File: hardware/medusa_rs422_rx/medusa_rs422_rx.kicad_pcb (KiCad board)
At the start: 2 copper layers, 42 x 50 mm, 16 parts, among them J1 HEADER_2X3, P1 RJ45X1, P2 RJ45X1, P3 BARRIER2, U1 UA9637A

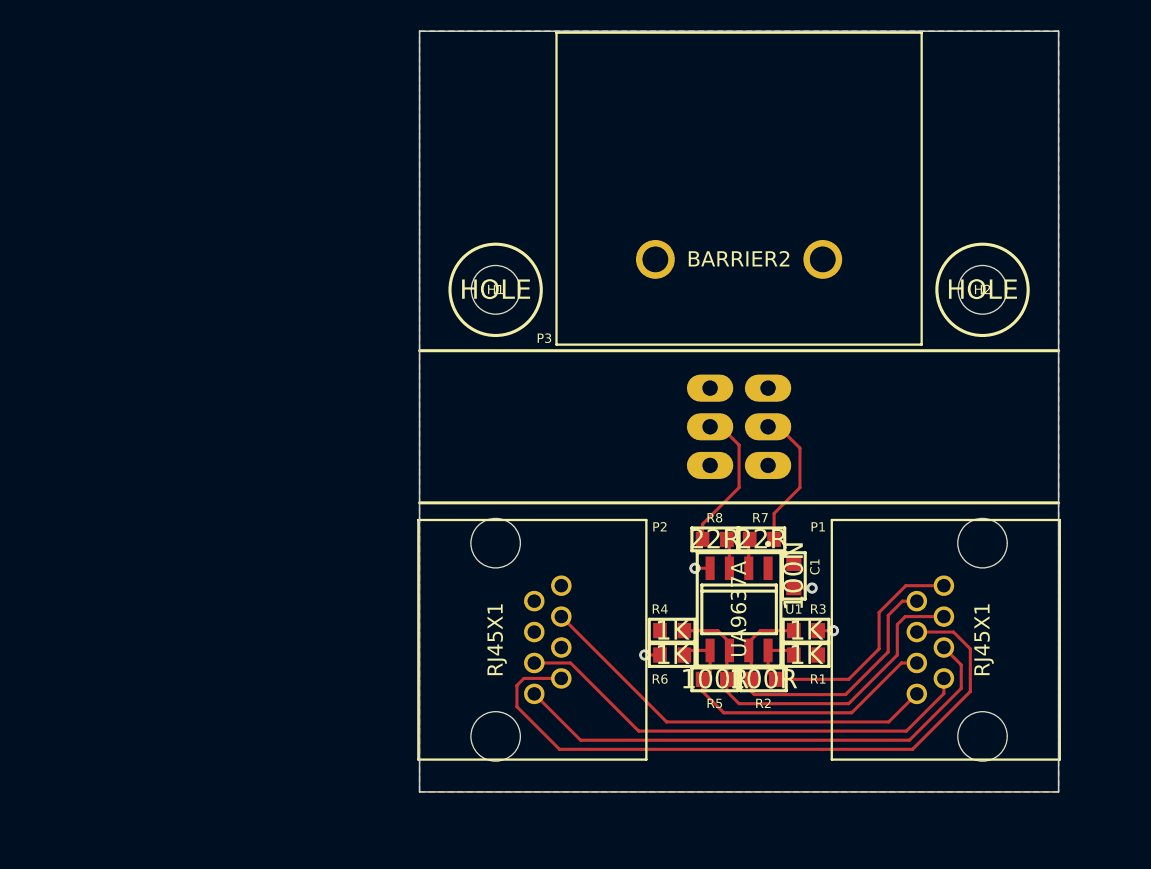
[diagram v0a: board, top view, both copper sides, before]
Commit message: Complete rebake of RX board.
Added ground isolation.
Changed receiver IC to better match transmitter specs.
Added somewhat sketchy termination + ground reference mechanism.
Removed RJ45 connectors and passthrough in favor of a single board with four channels and terminal blocks.
Added separate terminal blocks for power supply (+5V) and isolated power connections. If we run dedicated ground reference wires from the transmitters, this is where they'll connect.
Added optional power regulator for 3.3V operation, if we want to experiment with MCUs at the receivers.
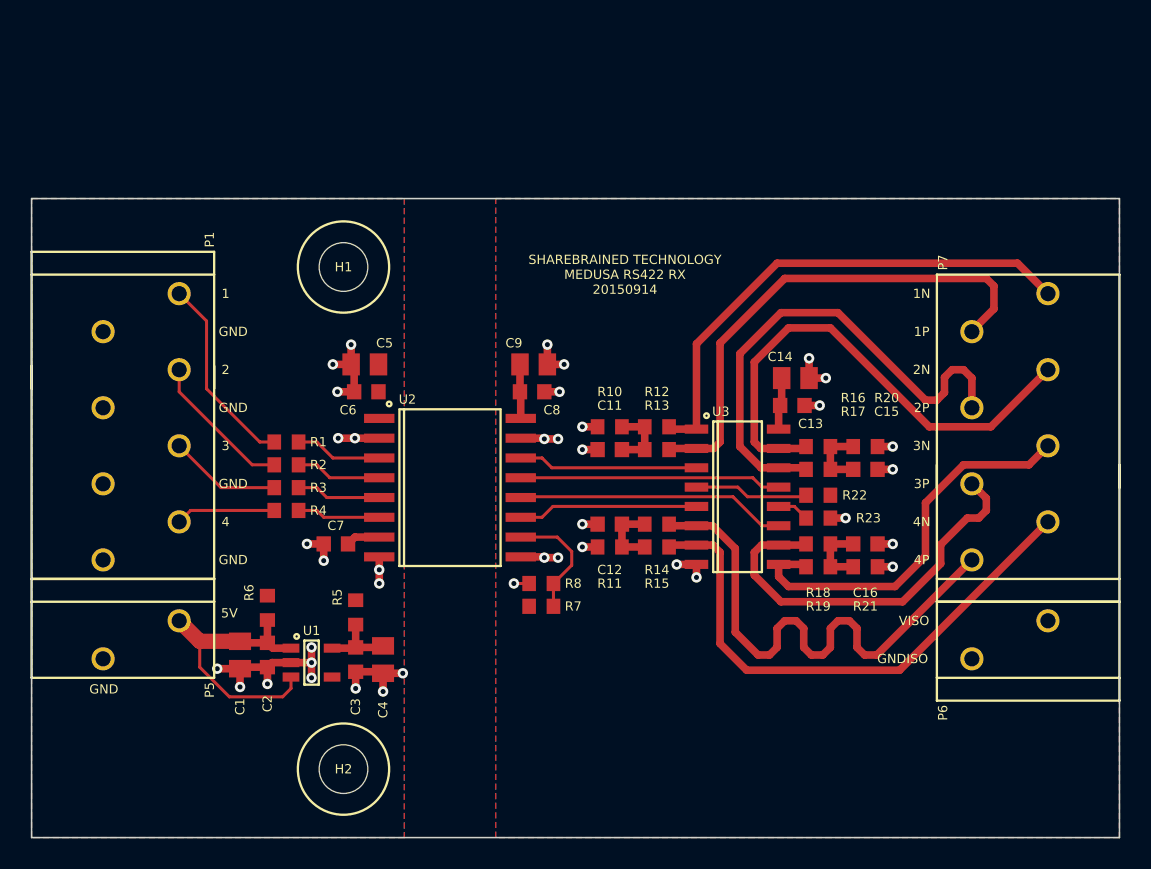
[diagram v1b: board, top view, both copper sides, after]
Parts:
- removed J1: HEADER_2X3, LED_STRIP_WS2812
- removed P2: RJ45X1, AMPHENOL_RJHSE5080
- removed P3: BARRIER2, ONSHORE_OSTYK55102030
- added C11: 10N, ipc_capc:IPC_CAPC1608X95N, F.Cu at (140.5, 101.5)
- added C12: 10N, ipc_capc:IPC_CAPC1608X95N, F.Cu at (140.5, 106.4)
- added C13: 100N, ipc_capc:IPC_CAPC1608X95N, F.Cu at (152.5, 98.6)
- added C14: 10U, ipc_capc:IPC_CAPC2012X140N, F.Cu at (152.7, 96.8)
- added C15: 10N, ipc_capc:IPC_CAPC1608X95N, F.Cu at (157.3, 102.8)
- added C16: 10N, ipc_capc:IPC_CAPC1608X95N, F.Cu at (157.3, 107.7)
- added C2: DNI, ipc_capc:IPC_CAPC1608X95N, F.Cu at (118.0, 115.0)
- added C3: DNI, ipc_capc:IPC_CAPC1608X95N, F.Cu at (123.8, 115.3)
- added C4: DNI, ipc_capc:IPC_CAPC2012X140N, F.Cu at (125.6, 115.3)
- added C5: 10U, ipc_capc:IPC_CAPC2012X140N, F.Cu at (124.4, 95.9)
- added C6: 100N, ipc_capc:IPC_CAPC1608X95N, F.Cu at (124.5, 97.7)
- added C7: 100N, ipc_capc:IPC_CAPC1608X95N, F.Cu at (122.5, 107.7)
- added C8: 100N, ipc_capc:IPC_CAPC1608X95N, F.Cu at (135.4, 97.7)
- added C9: 10U, ipc_capc:IPC_CAPC2012X140N, F.Cu at (135.5, 95.9)
- added P5: TERM2, phoenix:1990009, F.Cu at (108.5, 114.0)
- added P6: TERM2, phoenix:1990009, F.Cu at (168.0, 114.0)
- added P7: TERM8, phoenix:1990067, F.Cu at (168.0, 100.0)
- added R10: DNI, ipc_resc:IPC_RESC1608X55N, F.Cu at (140.5, 100.0)
- added R11: DNI, ipc_resc:IPC_RESC1608X55N, F.Cu at (140.5, 107.9)
- added R12: 50R, ipc_resc:IPC_RESC1608X55N, F.Cu at (143.6, 100.0)
- added R13: 50R, ipc_resc:IPC_RESC1608X55N, F.Cu at (143.6, 101.5)
- added R14: 50R, ipc_resc:IPC_RESC1608X55N, F.Cu at (143.6, 106.4)
- added R15: 50R, ipc_resc:IPC_RESC1608X55N, F.Cu at (143.6, 107.9)
- added R16: 50R, ipc_resc:IPC_RESC1608X55N, F.Cu at (154.2, 101.3)
- added R17: 50R, ipc_resc:IPC_RESC1608X55N, F.Cu at (154.2, 102.8)
- added R18: 50R, ipc_resc:IPC_RESC1608X55N, F.Cu at (154.2, 107.7)
- added R19: 50R, ipc_resc:IPC_RESC1608X55N, F.Cu at (154.2, 109.2)
- added R20: DNI, ipc_resc:IPC_RESC1608X55N, F.Cu at (157.3, 101.3)
- added R21: DNI, ipc_resc:IPC_RESC1608X55N, F.Cu at (157.3, 109.2)
- added R22: 0R, ipc_resc:IPC_RESC1608X55N, F.Cu at (154.2, 104.5)
- added R23: 0R, ipc_resc:IPC_RESC1608X55N, F.Cu at (154.2, 106.0)
- added U2: ADuM6404, ipc_soic:IPC_SOIC127P1030X265-16N, F.Cu at (130.0, 104.0)
- added U3: AM26LV32E, ipc_soic:IPC_SOIC127P600X175-16N, F.Cu at (148.9, 104.6)
- C1: value 100N -> DNI; footprint IPC_CAPC1608X95N -> ipc_capc:IPC_CAPC2012X140N
- H1, H2: footprint HOLE_3P2MM -> hole:HOLE_3P2MM
- P1: value RJ45X1 -> TERM8; footprint AMPHENOL_RJHSE5080 -> phoenix:1990067
- R1, R3, R4: value 1K -> 22R; footprint IPC_RESC1608X55N -> ipc_resc:IPC_RESC1608X55N
- R2: value 100R -> 22R; footprint IPC_RESC1608X55N -> ipc_resc:IPC_RESC1608X55N
- R5: value 100R -> DNI; footprint IPC_RESC1608X55N -> ipc_resc:IPC_RESC1608X55N
- R6: value 1K -> 0R; footprint IPC_RESC1608X55N -> ipc_resc:IPC_RESC1608X55N
- R7: value 22R -> DNI; footprint IPC_RESC1608X55N -> ipc_resc:IPC_RESC1608X55N
- R8: value 22R -> 0R; footprint IPC_RESC1608X55N -> ipc_resc:IPC_RESC1608X55N
- U1: value UA9637A -> DNI; footprint IPC_SOIC127P600X175-8N -> ipc_sot:IPC_SOT95P280X110-5N
- moved P1 58.2 mm to (108.5, 100.0), turned to 270 degrees
- moved H2 52.5 mm to (123.0, 122.5)
- moved R1 36.9 mm to (119.2, 101.0), turned to 180 degrees
- moved C1 36.8 mm to (116.2, 115.0)
- moved R3 35.4 mm to (119.2, 104.0)
- moved R2 34.4 mm to (119.2, 102.5), turned to 180 degrees
- moved U1 28.3 mm to (120.9, 115.5), turned to 0 degrees
- moved R6 26.8 mm to (118.0, 111.9), turned to 270 degrees
- moved R4 26.6 mm to (119.2, 105.5)
- moved R5 24.0 mm to (123.8, 112.2), turned to 270 degrees
- moved R7 15.2 mm to (136.0, 111.8), turned to 180 degrees
- moved R8 11.8 mm to (136.0, 110.3)
- moved H1 10.1 mm to (123.0, 89.5)
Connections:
- P1 pad 1: /RX1P -> GND
- P1 pad 2: /RX1N -> /RX4R
- P1 pad 3: /RX2P -> GND
- P1 pad 4: /PT1N -> /RX3R
- P1 pad 5: /PT1P -> GND
- P1 pad 6: /RX2N -> /RX2R
- P1 pad 7: /PT2P -> GND
- P1 pad 8: /PT2N -> /RX1R
- R1 pad 1: /RX1P -> /RX1
- R1 pad 2: +5V -> /RX1R
- R2 pad 1: /RX1N -> /RX2
- R2 pad 2: /RX1P -> /RX2R
- R3 pad 1: GND -> /RX3
- R3 pad 2: /RX1N -> /RX3R
- R4 pad 1: /RX2P -> /RX4
- R4 pad 2: +5V -> /RX4R
- R5 pad 1: /RX2N -> /VDD1
- R5 pad 2: /RX2P -> +3.3V
- R6 pad 1: GND -> /VDD1
- R6 pad 2: /RX2N -> +5V
- R7 pad 1: Net-<R7-Pad1> -> /VSEL
- R7 pad 2: /DI_B -> /VISO
- R8 pad 1: Net-<R8-Pad1> -> /VSEL
- R8 pad 2: /DI_A -> /GNDISO
- U1 pad 2: Net-<R7-Pad1> -> GND
- U1 pad 3: Net-<R8-Pad1> -> +5V
- U1 pad 4: GND -> (no net)
- U1 pad 5: /RX2N -> +3.3V
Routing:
- net /PT1N: track 43.8 -> 0.00 mm
- net /RX4P: track 0.00 -> 35.9 mm
- net /RX4N: track 0.00 -> 35.9 mm
- net /PT1P: track 33.9 -> 0.00 mm
- net /PT2P: track 30.8 -> 0.00 mm
- net /PT2N: track 27.0 -> 0.00 mm
- net /RX3N: track 0.00 -> 26.5 mm
- net /RX3P: track 0.00 -> 26.5 mm
- net GND: track 4.19 -> 28.2 mm, vias 4 -> 18
- net /GNDISO: track 0.00 -> 23.9 mm, vias 0 -> 22
- net +5V: track 0.00 -> 19.1 mm
- net /RX3ISO: track 0.00 -> 17.8 mm
- net /RX2ISO: track 0.00 -> 17.2 mm
- net /RX1P: track 18.9 -> 33.6 mm
- net /RX1R: track 0.00 -> 12.9 mm
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- added copper zone on B.Cu, net /GNDISO
- added copper zone on F.Cu, net /VDD1
- added copper zone on F.Cu, net /VISO
- removed copper zone on F.Cu, net +5V
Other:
- board size 42 x 50 mm -> 71.5 x 42 mm
- net class Default: clearance 0.2032 -> 0.2; trace_width 0.2032 -> 0.2; via_dia 0.7366 -> 0.6858; via_drill 0.381 -> 0.3302
- rule trace_clearance: 0.2032 -> 0.2
- rule trace_min: 0.2032 -> 0.2
- rule via_min_drill: 0.381 -> 0.3302
- rule via_min_size: 0.7366 -> 0.6858
- board text added: "1"
- board text added: "1N"
- board text added: "1P"
- board text added: "2"
- board text added: "2N"
- board text added: "2P"
- board text added: "3"
- board text added: "3N"
- board text added: "3P"
- board text added: "4"
- board text added: "4N"
- board text added: "4P"
- board text added: "GNDISO"
- board text added: "SHAREBRAINED TECHNOLOGY MEDUSA RS422 RX 20150914"
- board text added: "VISO"
- board text removed: "20131010"
- board text removed: "DA"
- board text removed: "DB"
- board text removed: "Medusa RX2"
- board text removed: "ShareBrained Technology, Inc."
- board text removed: "www.sharebrained.com"
